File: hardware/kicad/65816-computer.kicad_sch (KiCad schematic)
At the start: 0 parts

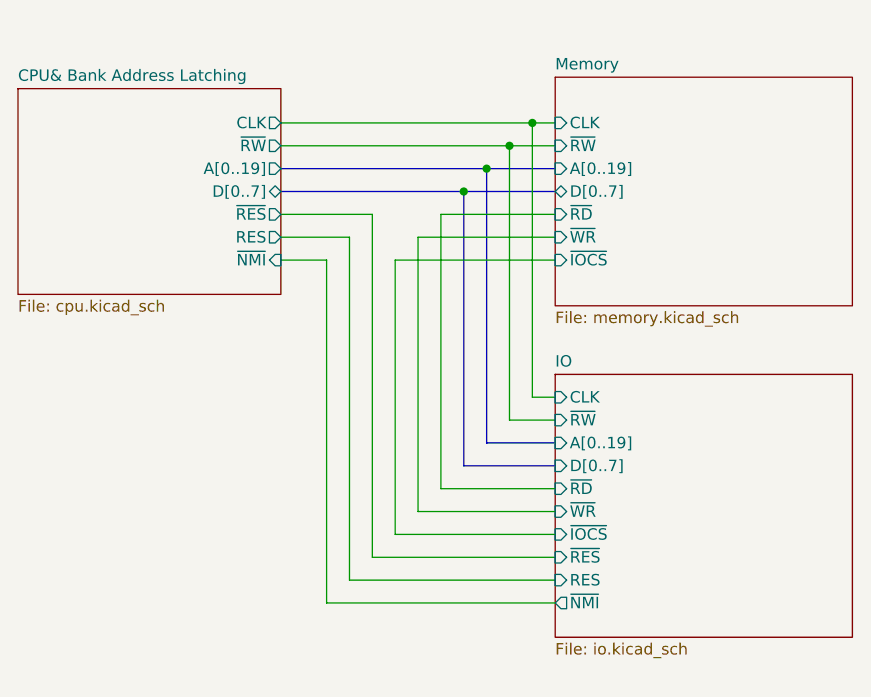
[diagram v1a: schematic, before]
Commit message: update schematic, add draft PCB
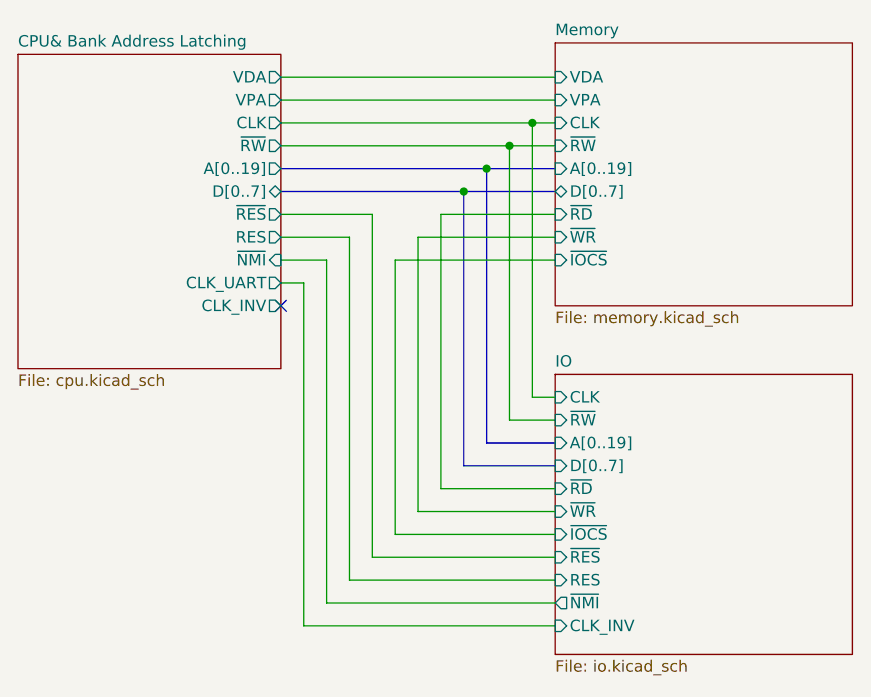
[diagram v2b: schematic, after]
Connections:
- no-connect marks 0 -> 1
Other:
- sheet CPU& Bank Address Latching ports: added CLK_INV, CLK_UART, VDA, VPA; removed none
- sheet IO ports: added CLK_INV; removed none
- sheet Memory ports: added VDA, VPA; removed none
